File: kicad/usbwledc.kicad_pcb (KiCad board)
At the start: 2 copper layers, 30 x 35 mm, 31 parts, among them J1 5V PAD, J10 USB_C_Receptacle_USB2.0, J2 D1 PAD, J3 GND PAD, J4 5V PAD, J5 D2 PAD, J6 GND PAD, J7 Accessories, SW1 FLASH_SW, U1 CH340N, U2 AMS1117-3.3, U3 ESP32-WROOM-32

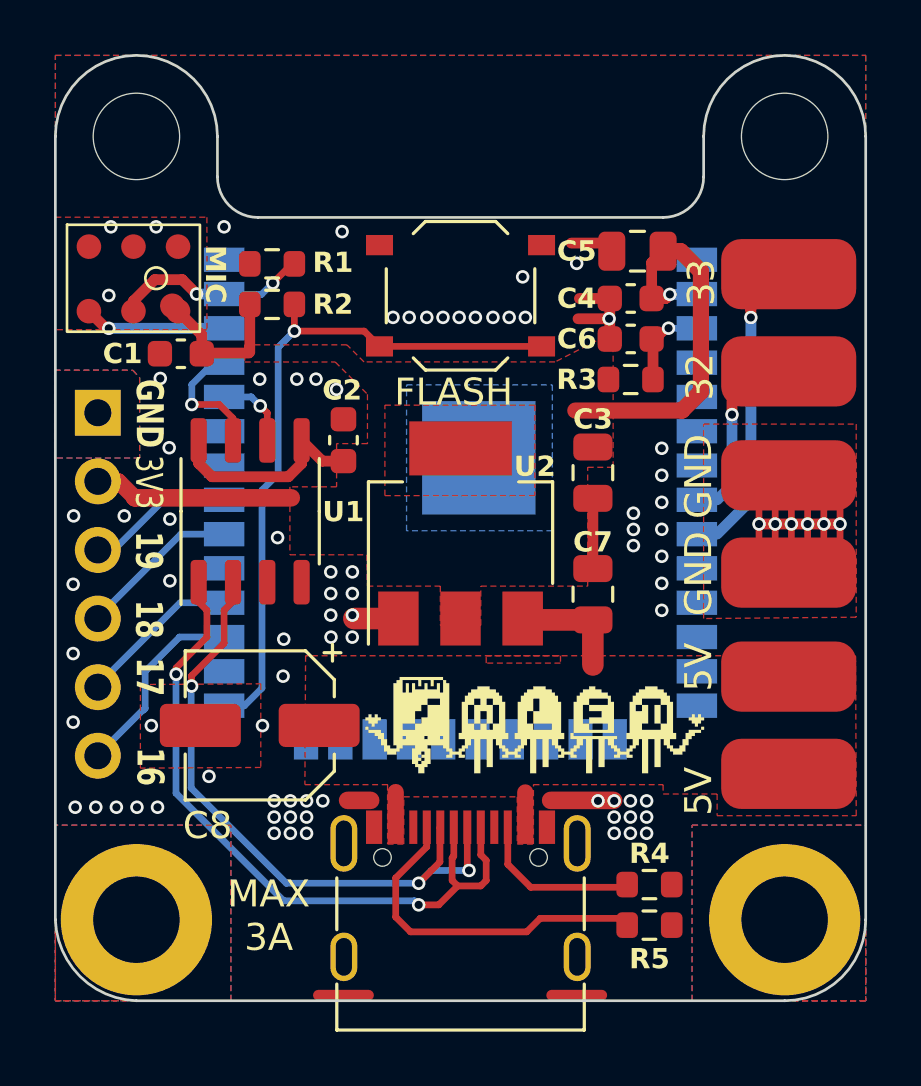
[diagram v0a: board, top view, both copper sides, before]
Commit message: update to Revision 1.2
Updated:
ESP32-WROOM-32 to ESP32-WROOM-32E
Changed CH340N to CH340C with Auto reset function
Changed components from 0805 to 0603/0402
Updated JLCPC component C8 to C7469983

Added:
SN74LVC2T45DCUR Levelshifter from 3.3V to 5V
USB Data ESD protection
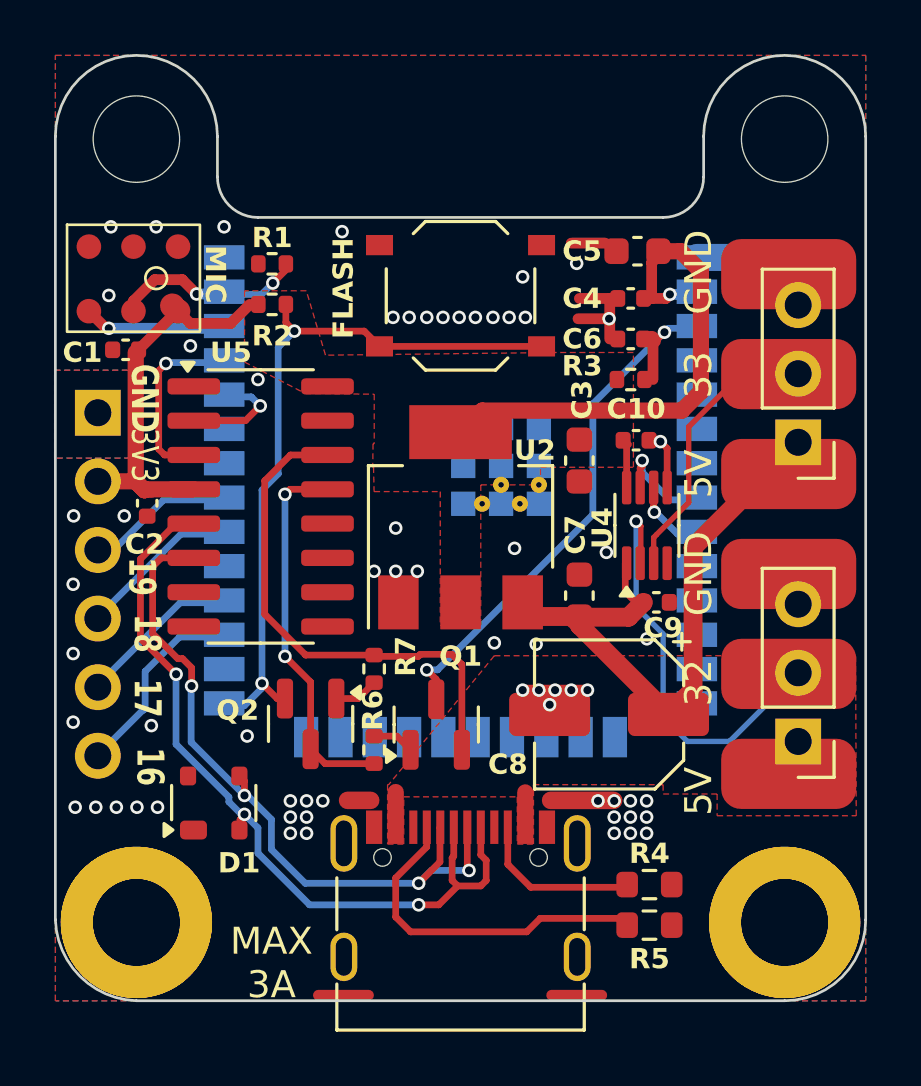
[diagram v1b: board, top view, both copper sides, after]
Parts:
- removed G***: LOGO, LOGO
- removed U1: CH340N, Package_SO:SOP-8_3.9x4.9mm_P1.27mm
- added ?: , , F.Cu at (57.0, 62.1)
- added ?: , , F.Cu at (33.0, 62.1)
- added C10: 100nF, Capacitor_SMD:C_0402_1005Metric, F.Cu at (51.5, 44.2)
- added C9: 100nF, Capacitor_SMD:C_0402_1005Metric, F.Cu at (52.2, 50.2)
- added D1: SP0503BAHT, Package_TO_SOT_SMD:SOT-143, F.Cu at (35.9, 57.7)
- added J8: Conn_01x03_Pin, Connector_PinHeader_2.54mm:PinHeader_1x03_P2.54mm_Vertical, F.Cu at (57.5, 55.4)
- added J9: Conn_01x03_Pin, Connector_PinHeader_2.54mm:PinHeader_1x03_P2.54mm_Vertical, F.Cu at (57.5, 44.3)
- added Q1: L8050QLT1G, Package_TO_SOT_SMD:SOT-23, F.Cu at (44.1, 54.8)
- added Q2: L8050QLT1G, Package_TO_SOT_SMD:SOT-23, F.Cu at (39.5, 54.8)
- added R6: 10k, Resistor_SMD:R_0402_1005Metric, F.Cu at (41.8, 55.7)
- added R7: 10k, Resistor_SMD:R_0402_1005Metric, F.Cu at (41.8, 52.7)
- added U4: SN74LVC2T45DCUR, Package_SO:VSSOP-8_2.3x2mm_P0.5mm, F.Cu at (51.9, 47.4)
- added U5: CH340C, Package_SO:SOIC-16_3.9x9.9mm_P1.27mm, F.Cu at (37.6, 46.7)
- C1, C2, C4, C6: footprint Capacitor_SMD:C_0603_1608Metric -> Capacitor_SMD:C_0402_1005Metric
- C3, C5, C7: footprint Capacitor_SMD:C_0805_2012Metric -> Capacitor_SMD:C_0603_1608Metric
- R1, R2, R3: footprint Resistor_SMD:R_0603_1608Metric -> Resistor_SMD:R_0402_1005Metric
- U3: value ESP32-WROOM-32 -> ESP32-WROOM-32E-N4; footprint RF_Module:ESP32-WROOM-32 -> RF_Module:ESP32-WROOM-32E
- moved C8 12.9 mm to (50.5, 54.4)
- moved J2 11.2 mm to (57.1, 52.9)
- moved C2 7.63 mm to (33.4, 46.6), turned to 90 degrees
- moved J4 7.50 mm to (57.1, 45.5)
- moved J6 7.45 mm to (57.1, 38.1)
- moved J5 3.70 mm to (57.1, 41.8)
- moved U3 3.07 mm to (45.0, 42.7)
- moved C1 2.05 mm to (32.6, 40.9)
- moved C3 0.67 mm to (49.4, 45.0)
- moved U2 0.60 mm to (45.0, 47.1)
- moved C7 0.50 mm to (49.4, 50.0)
- moved H1 0.10 mm to (33.0, 62.1)
- moved H2 0.10 mm to (57.0, 62.1)
- moved H3 0.10 mm to (57.0, 33.1)
- moved H4 0.10 mm to (33.0, 33.1)
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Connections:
- net Net-(U3-EN) renamed EN
- J2 pad 1: STRIP_DATA_1 -> STRIP_DATA_LS_1
- J5 pad 1: STRIP_DATA_2 -> STRIP_DATA_LS_2
- R2 pad 1: +3V3 -> FLASH
- R2 pad 2: FLASH -> +3V3
- U3 pad 12: RELAY -> unconnected-(U3-IO27-Pad12)
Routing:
- net +5V: track 6.52 -> 26.2 mm
- net RTS: track 0.00 -> 19.3 mm
- net EN: track 3.14 -> 20.7 mm, vias 1 -> 2
- net STRIP_DATA_LS_1: track 0.00 -> 15.7 mm, vias 0 -> 1
- net DTR: track 0.00 -> 14.1 mm, vias 0 -> 2
- net STRIP_DATA_LS_2: track 0.00 -> 10.1 mm
- net STRIP_DATA_2: track 9.59 -> 2.83 mm
- net GND: track 27.0 -> 20.6 mm, vias 85 -> 64
- net D+: track 26.3 -> 29.9 mm, vias 2 -> 3
- net D-: track 24.2 -> 27.0 mm, vias 3 -> 4
- net TX: track 4.83 -> 6.84 mm
- net Net-(Q2-B): track 0.00 -> 1.64 mm
- net Net-(Q1-B): track 0.00 -> 1.56 mm
- net FLASH: track 25.8 -> 27.1 mm, vias 1 -> 2
- net RX: track 2.86 -> 4.16 mm
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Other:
- board text added: "Yannik25"
- board text added: "v1.2"
- board text removed: "NANDXOR"
- board text removed: "v1.1"

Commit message: fix resistor placement instead of caps, replace mic, fix count of components
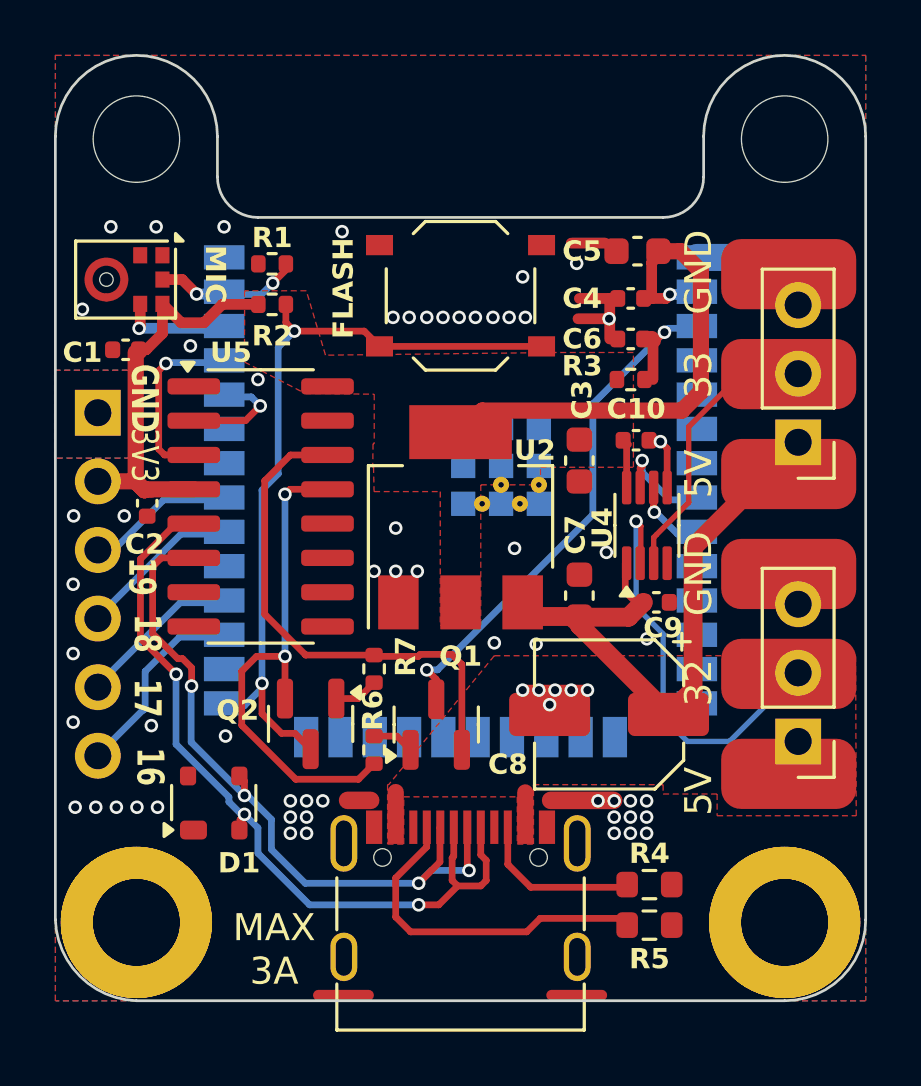
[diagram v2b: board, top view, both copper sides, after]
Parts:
- MK1: value GSA4737 -> ICS-43434; footprint microphone:Microphone-6pin -> Sensor_Audio:InvenSense_ICS-43434-6_3.5x2.65mm
- moved MK1 2.83 mm to (32.6, 38.3)
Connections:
- MK1 pad 1: GND -> unconnected-(MK1-WS-Pad1)
- MK1 pad 2: unconnected-(MK1-WS-Pad2) -> GND
- MK1 pad 5: I2S_SD -> +3V3
- MK1 pad 6: +3V3 -> I2S_SD
- Q2 pad 2: FLASH -> DTR
- Q2 pad 3: DTR -> FLASH
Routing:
- net DTR: track 14.1 -> 19.1 mm
- net FLASH: track 27.1 -> 29.4 mm
- net I2S_SD: track 7.18 -> 5.40 mm
- net I2S_SCK: track 5.27 -> 4.07 mm
- net +3V3: track 35.3 -> 36.3 mm
